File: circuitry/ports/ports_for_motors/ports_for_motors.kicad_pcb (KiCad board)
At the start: 2 copper layers, 23.5 x 23.5 mm, 2 parts, among them J1 RJ12, J2 Conn_01x06_Pin

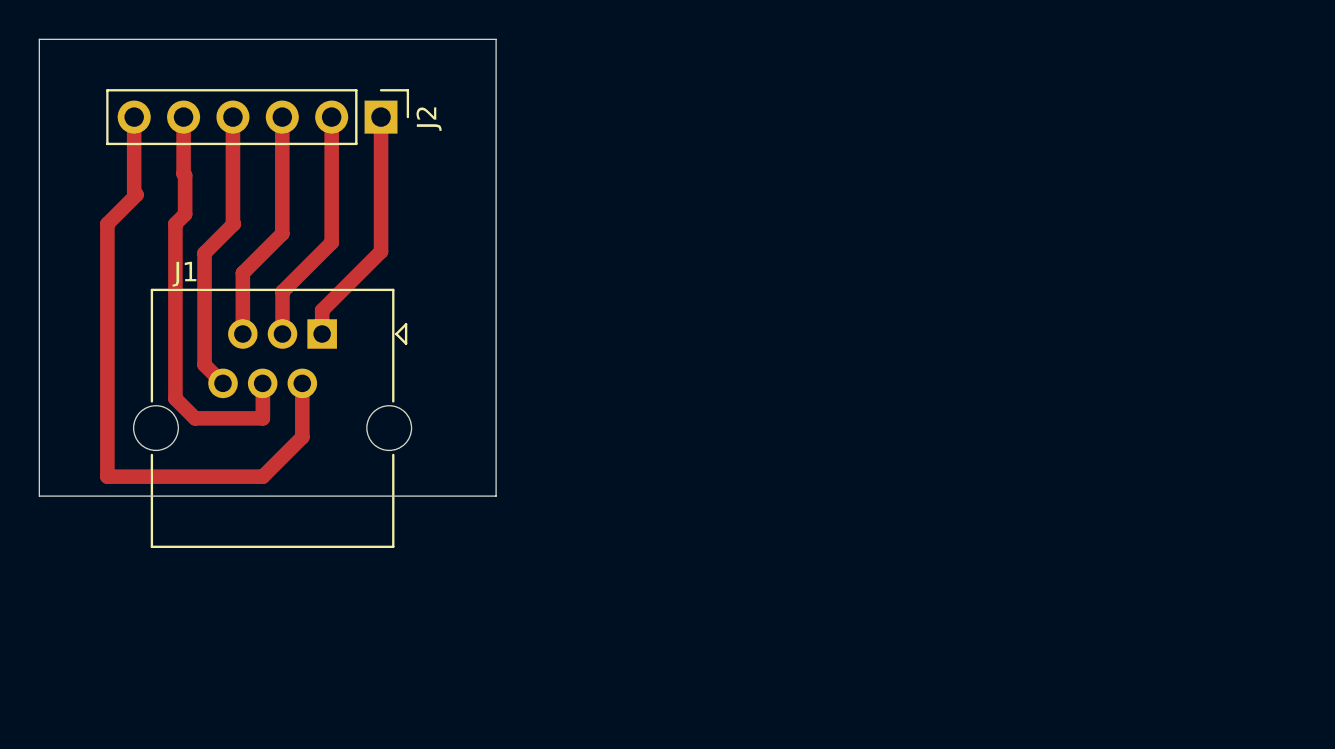
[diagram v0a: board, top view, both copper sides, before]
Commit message: main.ino: added TODO and comments, expanded code, added "reference code" for further expantion; the rest: updated circuitry, started moving to vscode
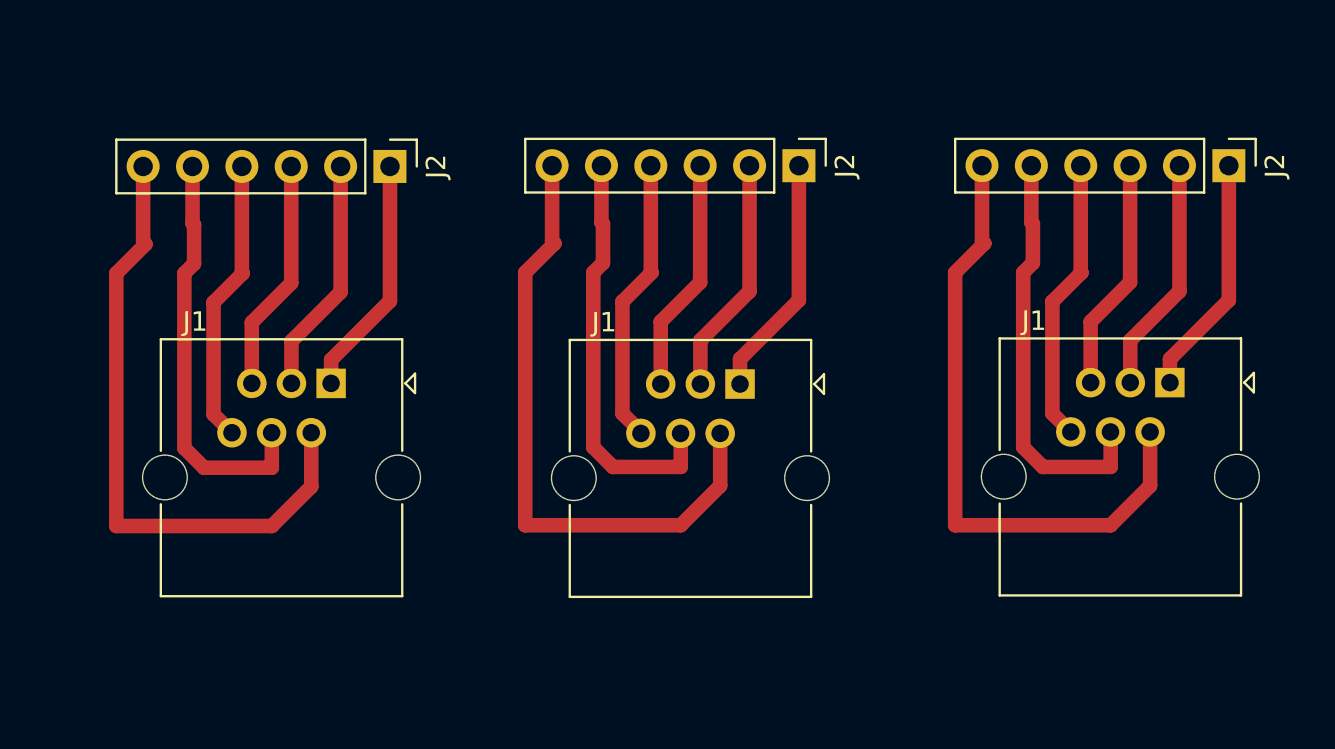
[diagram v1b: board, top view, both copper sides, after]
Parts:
- added J1: RJ12, Connector_RJ:RJ25_Wayconn_MJEA-660X1_Horizontal, F.Cu at (77.7, 35.2)
- added J1: RJ12, Connector_RJ:RJ25_Wayconn_MJEA-660X1_Horizontal, F.Cu at (55.5, 35.2)
- added J2: Conn_01x06_Pin, Connector_PinHeader_2.54mm:PinHeader_1x06_P2.54mm_Vertical, F.Cu at (80.7, 24.0)
- added J2: Conn_01x06_Pin, Connector_PinHeader_2.54mm:PinHeader_1x06_P2.54mm_Vertical, F.Cu at (58.6, 24.0)
- moved J1 2.58 mm to (34.5, 35.2)
- moved J2 2.58 mm to (37.5, 24.0)
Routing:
- net Net-(J2-Pin_6): track 32.8 -> 98.4 mm
- net Net-(J2-Pin_5): track 21.5 -> 64.4 mm
- net Net-(J2-Pin_4): track 14.7 -> 44.2 mm
- net Net-(J2-Pin_1): track 12.4 -> 37.2 mm
- net Net-(J2-Pin_2): track 12.2 -> 36.6 mm
- net Net-(J2-Pin_3): track 12.0 -> 36.0 mm
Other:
- board outline removed

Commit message: finished first prototype ready to test
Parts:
- removed the J1 at (77.7, 35.2)
- removed the J2 at (80.7, 24.0)
- moved J1 10.3 mm to (65.6, 37.7)
- moved J2 10.3 mm to (68.6, 26.5)
- moved J1 10.3 mm to (44.5, 37.7)
- moved J2 10.3 mm to (47.6, 26.5)
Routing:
- net Net-(J2-Pin_6): track 98.4 -> 65.6 mm
- net Net-(J2-Pin_5): track 64.4 -> 42.9 mm
- net Net-(J2-Pin_4): track 44.2 -> 29.5 mm
- net Net-(J2-Pin_1): track 37.2 -> 24.8 mm
- net Net-(J2-Pin_2): track 36.6 -> 24.4 mm
- net Net-(J2-Pin_3): track 36.0 -> 24.0 mm
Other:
- board outline added: 57.5 x 30.5 mm
